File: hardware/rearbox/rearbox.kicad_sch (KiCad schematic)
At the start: 22 parts, among them J1 STDC14, J2 ST-LINK, SW1 Reset, U1 LM4040C33FTA, U2 STM32G473RCTx, Y1 48MHz

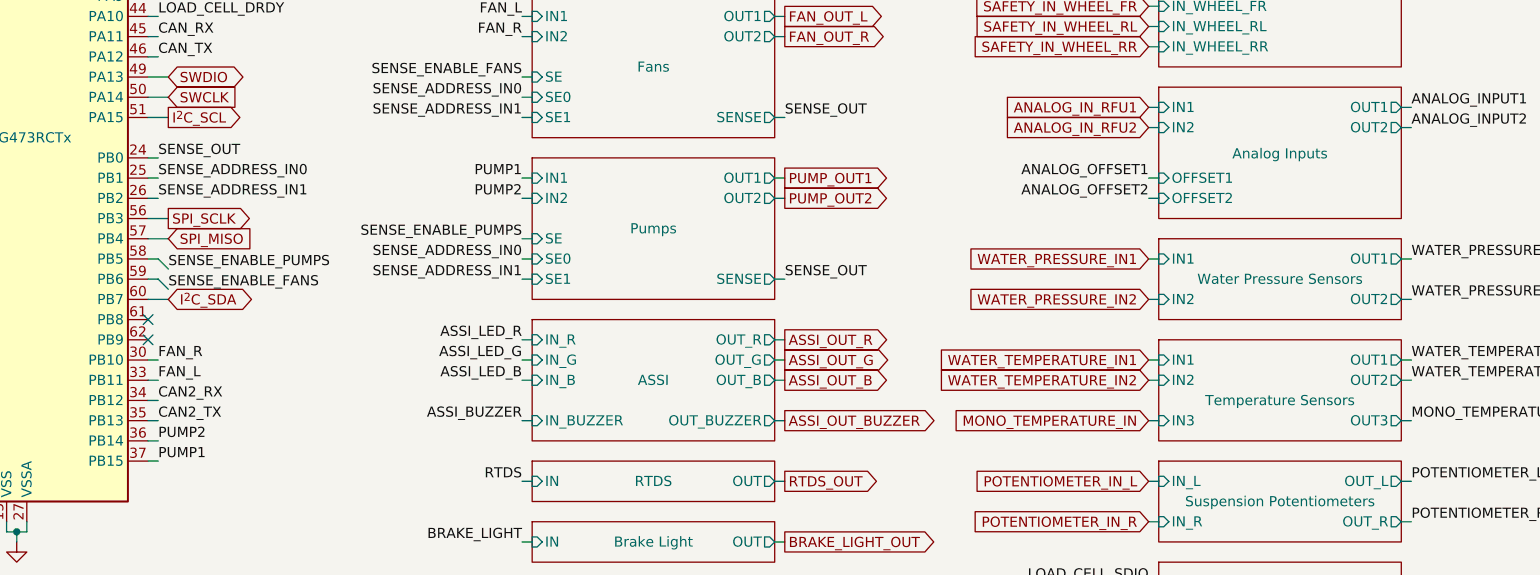
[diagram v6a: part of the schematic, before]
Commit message: Fix measurement bridges polarity
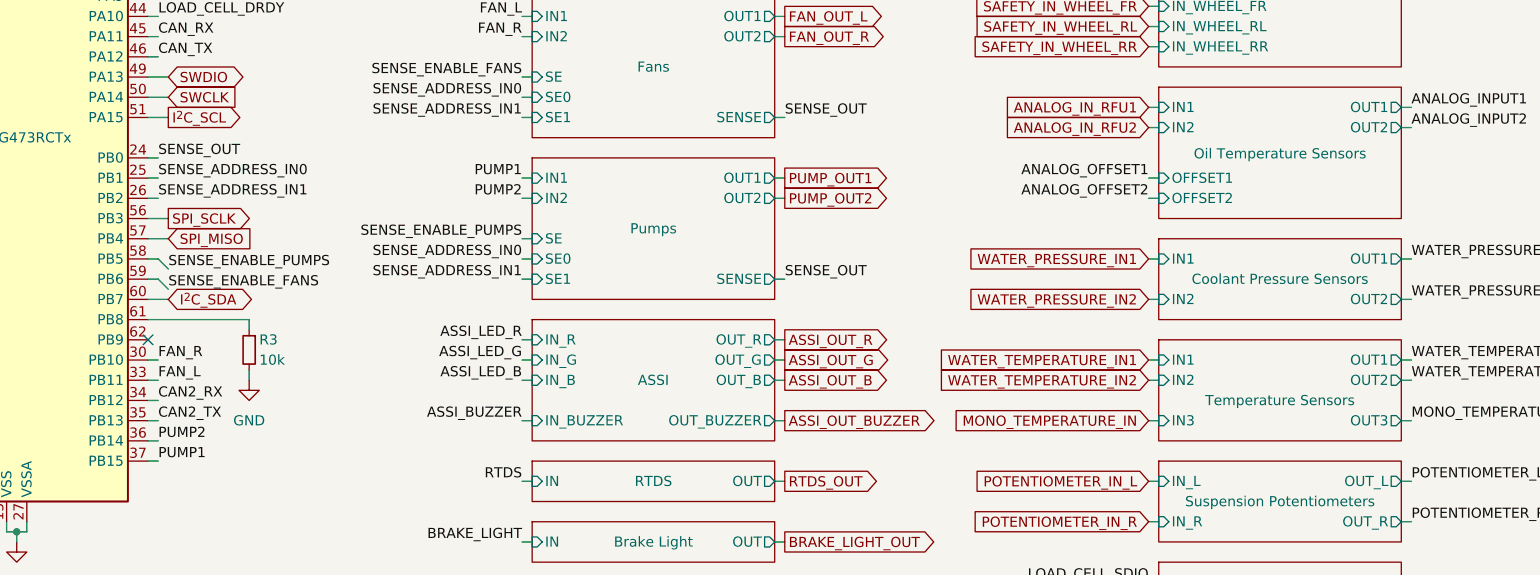
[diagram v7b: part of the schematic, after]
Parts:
- added R3: 10k, Resistor_SMD:R_0603_1608Metric, symbol Device:R_Small
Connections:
- net GND: now also R3.2
- net at U2.61 (PB8): now also R3.1
- no-connect marks 14 -> 13
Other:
- sheet Analog Inputs renamed Oil Temperature Sensors
- sheet Water Pressure Sensors renamed Coolant Pressure Sensors
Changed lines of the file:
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@@
   (title_block
     (title "Rearbox")
-    (date "2023-11-17")
+    (date "2024-04-28")
     (rev "${REVISION}")
     (company "Author: I. Kajdan")
@@
   (no_connect (at 64.77 54.61))
   (no_connect (at 46.99 138.43))
-  (no_connect (at 101.6 100.33))
   (no_connect (at 59.69 143.51))
   (no_connect (at 35.56 177.8))
@@
     (stroke (width 0) (type default))
   )
+  (wire (pts (xy 114.3 106.68) (xy 114.3 107.95))
+    (stroke (width 0) (type default))
+  )
   (wire (pts (xy 85.09 127) (xy 86.36 127))
     (stroke (width 0) (type default))
@@
     (stroke (width 0) (type default))
   )
+  (wire (pts (xy 114.3 100.33) (xy 114.3 101.6))
+    (stroke (width 0) (type default))
+  )
   (wire (pts (xy 227.33 133.35) (xy 228.6 133.35))
     (stroke (width 0) (type default))
@@
     (stroke (width 0) (type default))
   )
+  (wire (pts (xy 101.6 100.33) (xy 114.3 100.33))
+    (stroke (width 0) (type default))
+  )
   (wire (pts (xy 64.77 80.01) (xy 66.04 80.01))
     (stroke (width 0) (type default))
@@
     )
   )
+  (global_label "SAFETY_IN_AS_TS_ON" (shape input) (at 227.33 53.34 180) (fields_autoplaced)
+    (effects (font (size 1.27 1.27)) (justify right))
+    (property "Intersheetrefs" "${INTERSHEET_REFS}" (at 204.811 53.34 0)
+      (effects (font (size 1.27 1.27)) (justify right) hide)
+    )
+  )
   (global_label "CAN-" (shape bidirectional) (at 181.61 45.72 0) (fields_autoplaced)
     (effects (font (size 1.27 1.27)) (justify left))
@@
     )
   )
-  (global_label "SAFETY_IN_AS_TS_ON" (shape input) (at 227.33 53.34 180) (fields_autoplaced)
-    (effects (font (size 1.27 1.27) (color 179 0 27 1)) (justify right))
-    (property "Intersheetrefs" "${INTERSHEET_REFS}" (at 204.811 53.34 0)
-      (effects (font (size 1.27 1.27)) (justify right) hide)
-    )
-  )
   (global_label "SAFETY_IN_WHEEL_FL" (shape input) (at 227.33 58.42 180) (fields_autoplaced)
     (effects (font (size 1.27 1.27)) (justify right))
@@
     )
   )
+  (symbol (lib_id "power:GND") (at 114.3 107.95 0) (unit 1)
+    (in_bom yes) (on_board yes) (dnp no)
+    (property "Reference" "#PWR018" (at 114.3 114.3 0)
+      (effects (font (size 1.27 1.27)) hide)
+    )
+    (property "Value" "GND" (at 114.3 113.03 0)
+      (effects (font (size 1.27 1.27)))
+    )
+    (property "Footprint" "" (at 114.3 107.95 0)
+      (effects (font (size 1.27 1.27)) hide)
+    )
+    (property "Datasheet" "" (at 114.3 107.95 0)
+      (effects (font (size 1.27 1.27)) hide)
+    )
+    (pin "1")
+    (instances
+      (project "rearbox"
+        (path "/b652b05a-4e3d-4ad1-b032-18886abe7d45"
+          (reference "#PWR018") (unit 1)
+        )
+      )
+    )
+  )
   (symbol (lib_id "Connector:TestPoint_Small") (at 146.05 173.99 0) (unit 1)
     (in_bom yes) (on_board yes) (dnp no)
@@
     )
   )
+  (symbol (lib_id "Device:R_Small") (at 114.3 104.14 0) (mirror y) (unit 1)
+    (in_bom yes) (on_board yes) (dnp no)
+    (property "Reference" "R3" (at 115.57 102.87 0)
+      (effects (font (size 1.27 1.27)) (justify right))
+    )
+    (property "Value" "10k" (at 115.57 105.41 0)
+      (effects (font (size 1.27 1.27)) (justify right))
+    )
+    (property "Footprint" "Resistor_SMD:R_0603_1608Metric" (at 114.3 104.14 0)
+      (effects (font (size 1.27 1.27)) hide)
+    )
+    (property "Datasheet" "~" (at 114.3 104.14 0)
+      (effects (font (size 1.27 1.27)) hide)
+    )
+    (pin "1")
+    (pin "2")
+    (instances
+      (project "rearbox"
+        (path "/b652b05a-4e3d-4ad1-b032-18886abe7d45"
+          (reference "R3") (unit 1)
+        )
+      )
+    )
+  )
   (symbol (lib_id "Connector:TestPoint_Small") (at 97.79 173.99 0) (unit 1)
     (in_bom yes) (on_board yes) (dnp no)
@@
   (symbol (lib_id "power:+3.3V") (at 125.73 172.72 0) (unit 1)
     (in_bom yes) (on_board yes) (dnp no)
-    (property "Reference" "#PWR018" (at 125.73 176.53 0)
+    (property "Reference" "#PWR019" (at 125.73 176.53 0)
       (effects (font (size 1.27 1.27)) hide)
     )
@@
       (project "rearbox"
         (path "/b652b05a-4e3d-4ad1-b032-18886abe7d45"
-          (reference "#PWR018") (unit 1)
+          (reference "#PWR019") (unit 1)
         )
       )
@@
   (symbol (lib_id "power:VDDA") (at 146.05 172.72 0) (unit 1)
     (in_bom yes) (on_board yes) (dnp no)
-    (property "Reference" "#PWR019" (at 146.05 176.53 0)
+    (property "Reference" "#PWR020" (at 146.05 176.53 0)
       (effects (font (size 1.27 1.27)) hide)
     )
@@
       (project "rearbox"
         (path "/b652b05a-4e3d-4ad1-b032-18886abe7d45"
-          (reference "#PWR019") (unit 1)
+          (reference "#PWR020") (unit 1)
         )
       )
@@
   (symbol (lib_id "power:GND") (at 146.05 185.42 0) (unit 1)
     (in_bom yes) (on_board yes) (dnp no) (fields_autoplaced)
-    (property "Reference" "#PWR020" (at 146.05 191.77 0)
+    (property "Reference" "#PWR021" (at 146.05 191.77 0)
       (effects (font (size 1.27 1.27)) hide)
     )
@@
       (project "rearbox"
         (path "/b652b05a-4e3d-4ad1-b032-18886abe7d45"
-          (reference "#PWR020") (unit 1)
+          (reference "#PWR021") (unit 1)
         )
       )
@@
     (stroke (width 0.1524) (type solid))
     (fill (color 0 0 0 0.0000))
-    (property "Sheetname" "Analog Inputs" (at 243.84 78.74 0)
+    (property "Sheetname" "Oil Temperature Sensors" (at 243.84 78.74 0)
       (effects (font (size 1.27 1.27)) (justify top))
     )
@@
     (stroke (width 0.1524) (type solid))
     (fill (color 0 0 0 0.0000))
-    (property "Sheetname" "Water Pressure Sensors" (at 243.84 95.25 0)
+    (property "Sheetname" "Coolant Pressure Sensors" (at 243.84 95.25 0)
       (effects (font (size 1.27 1.27)))
     )
